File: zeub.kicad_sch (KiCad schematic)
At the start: 27 parts, among them J1 debug-port, J2 OLED-128x32, J5 Conn_01x03, J6 Conn_01x03, Q1 AO3401A, Q2 AO3401A, Q3 AO3401A, Q4 AO3401A, Q5 AO3401A, SW1 SKRHA, SW2 RotaryEncoder_Switch, U5 holyiot-18010-no-underside, U6 MT25QL128ABA1ESE

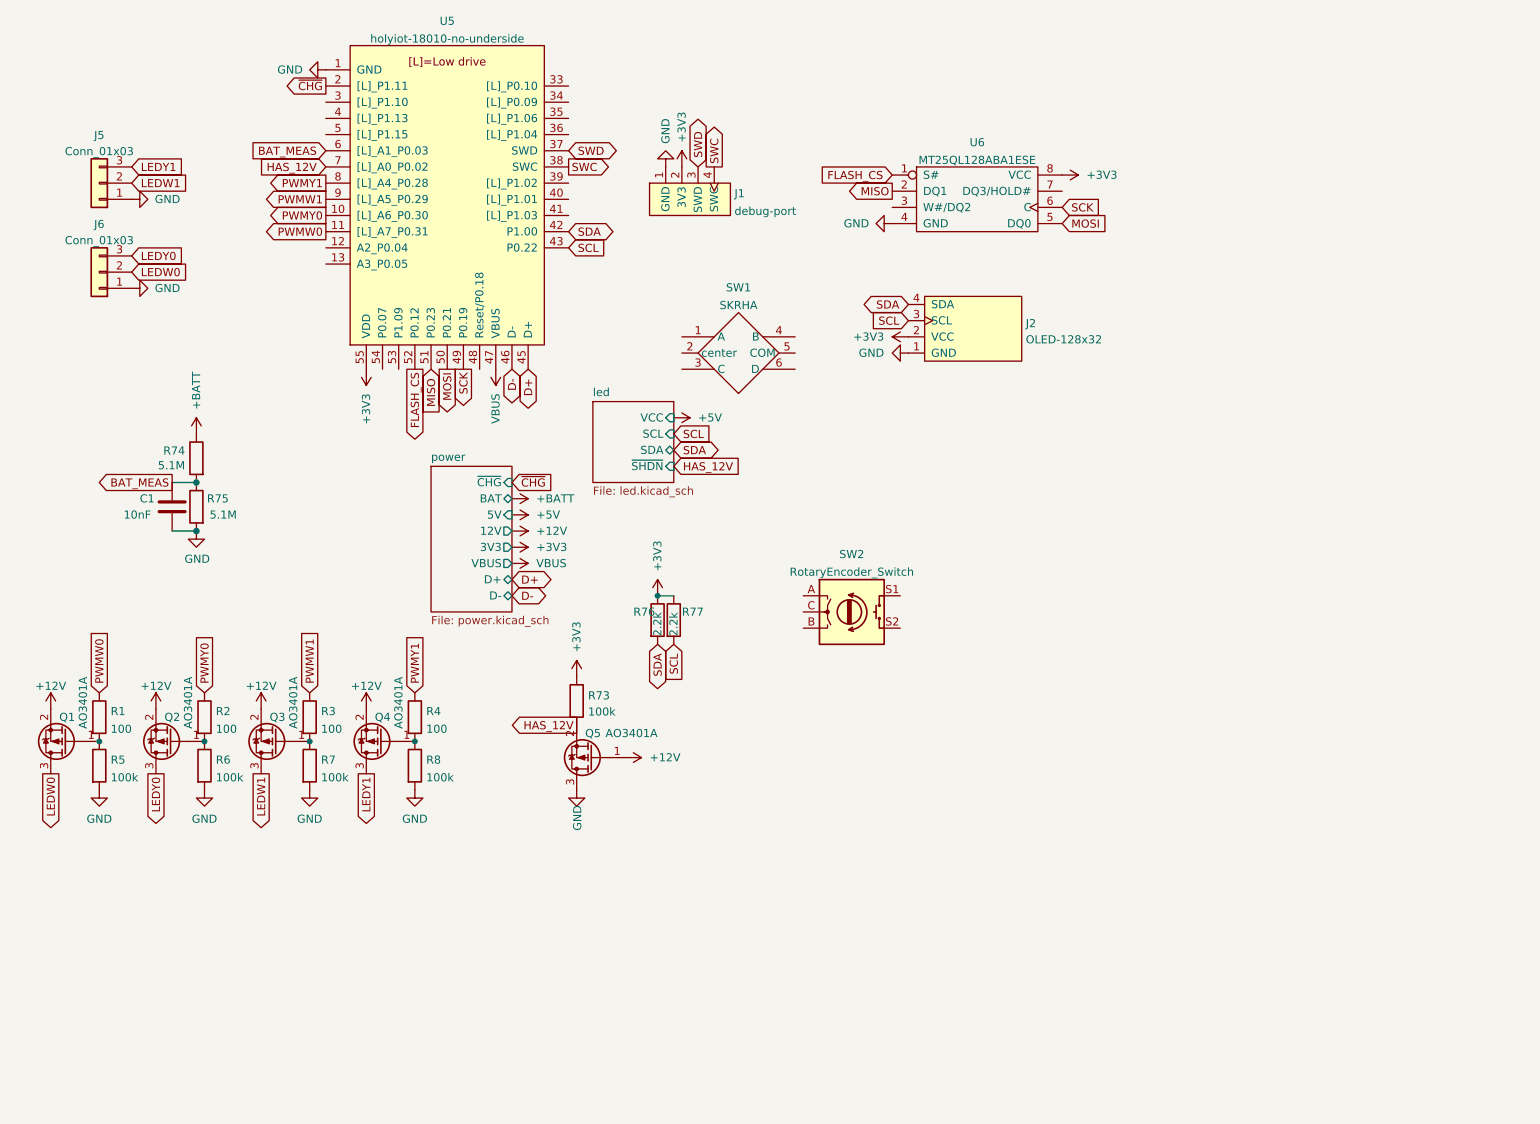
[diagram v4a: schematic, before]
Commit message: rid of LED driver resistors
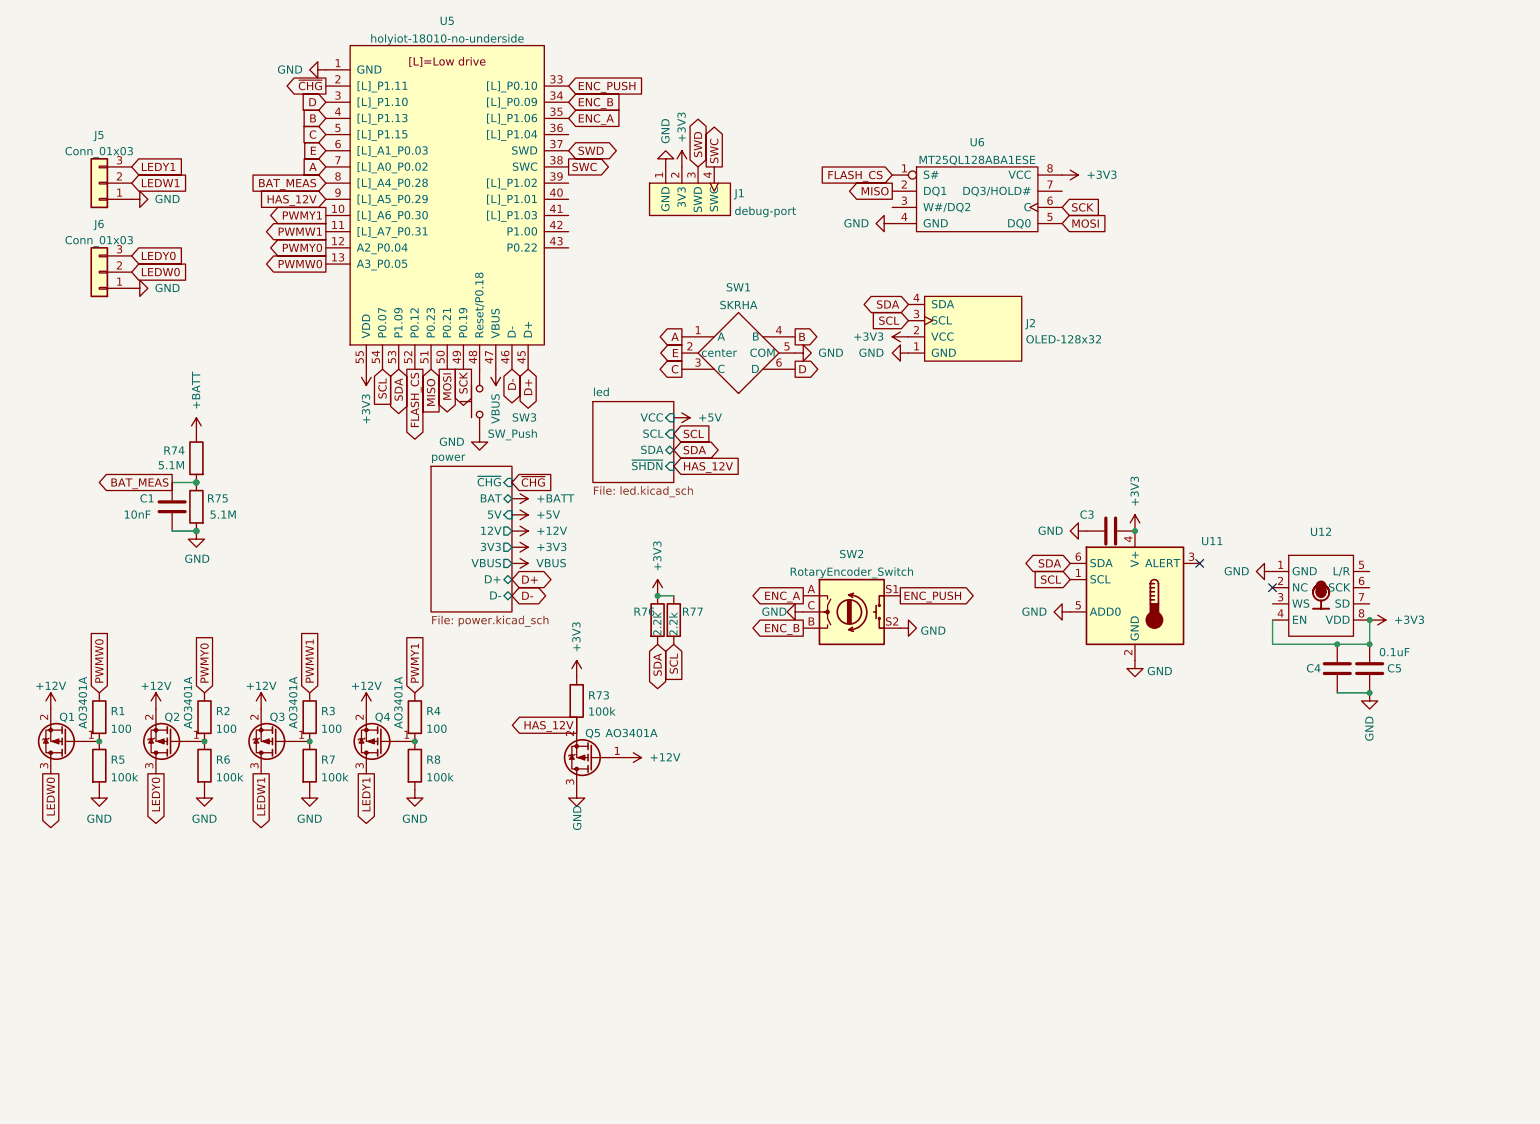
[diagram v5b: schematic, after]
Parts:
- added C3, C4: (no value), Capacitor_SMD:C_0603_1608Metric, symbol Device:C
- added C5: 0.1uF, Capacitor_SMD:C_0603_1608Metric, symbol Device:C
- added SW3: SW_Push, Button_Switch_SMD:SW_SPST_B3U-1000P, symbol Switch:SW_Push
- added U11: (no value), symbol ic:TMP117
- added U12: (no value), symbol ic:CMM4030D
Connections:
- net +3V3: now also C3.2, C4.2, C5.2, U11.4 (V+), U12.4 (EN), U12.8 (VDD)
- net BAT_MEAS: now also U5.8 ([L]_A4_P0.28); no longer U5.6 ([L]_A1_P0.03)
- net GND: now also SW1.5 (COM), SW2.C, SW2.S2, C3.1, C4.1, C5.1, SW3.1, U11.2 (GND), U11.5 (ADD0), U11.7 (GND), U12.1 (GND)
- net HAS_12V: now also U5.9 ([L]_A5_P0.29); no longer U5.7 ([L]_A0_P0.02)
- net PWMW0: now also U5.13 (A3_P0.05); no longer U5.11 ([L]_A7_P0.31)
- net PWMW1: now also U5.11 ([L]_A7_P0.31); no longer U5.9 ([L]_A5_P0.29)
- net PWMY0: now also U5.12 (A2_P0.04); no longer U5.10 ([L]_A6_P0.30)
- net PWMY1: now also U5.10 ([L]_A6_P0.30); no longer U5.8 ([L]_A4_P0.28)
- net SCL: now also U5.54 (P0.07), U11.1 (SCL); no longer U5.43 (P0.22)
- net SDA: now also U5.53 (P1.09), U11.6 (SDA); no longer U5.42 (P1.00)
- net A: now reaches SW1.1 (A)
- net A: now also U5.7 ([L]_A0_P0.02)
- net E: now reaches SW1.2 (center)
- net E: now also U5.6 ([L]_A1_P0.03)
- net C: now reaches SW1.3 (C)
- net C: now also U5.5 ([L]_P1.15)
- net B: now reaches SW1.4 (B)
- net B: now also U5.4 ([L]_P1.13)
- net D: now reaches SW1.6 (D)
- net D: now also U5.3 ([L]_P1.10)
- net ENC_A: now reaches SW2.A
- net ENC_A: now also U5.35 ([L]_P1.06)
- net ENC_B: now reaches SW2.B
- net ENC_B: now also U5.34 ([L]_P0.09)
- net ENC_PUSH: now reaches SW2.S1
- net ENC_PUSH: now also U5.33 ([L]_P0.10)
- net at U5.48 (Reset/P0.18): now also SW3.2
- no-connect marks 0 -> 2

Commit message: Added audio stuff; rerouted for prep
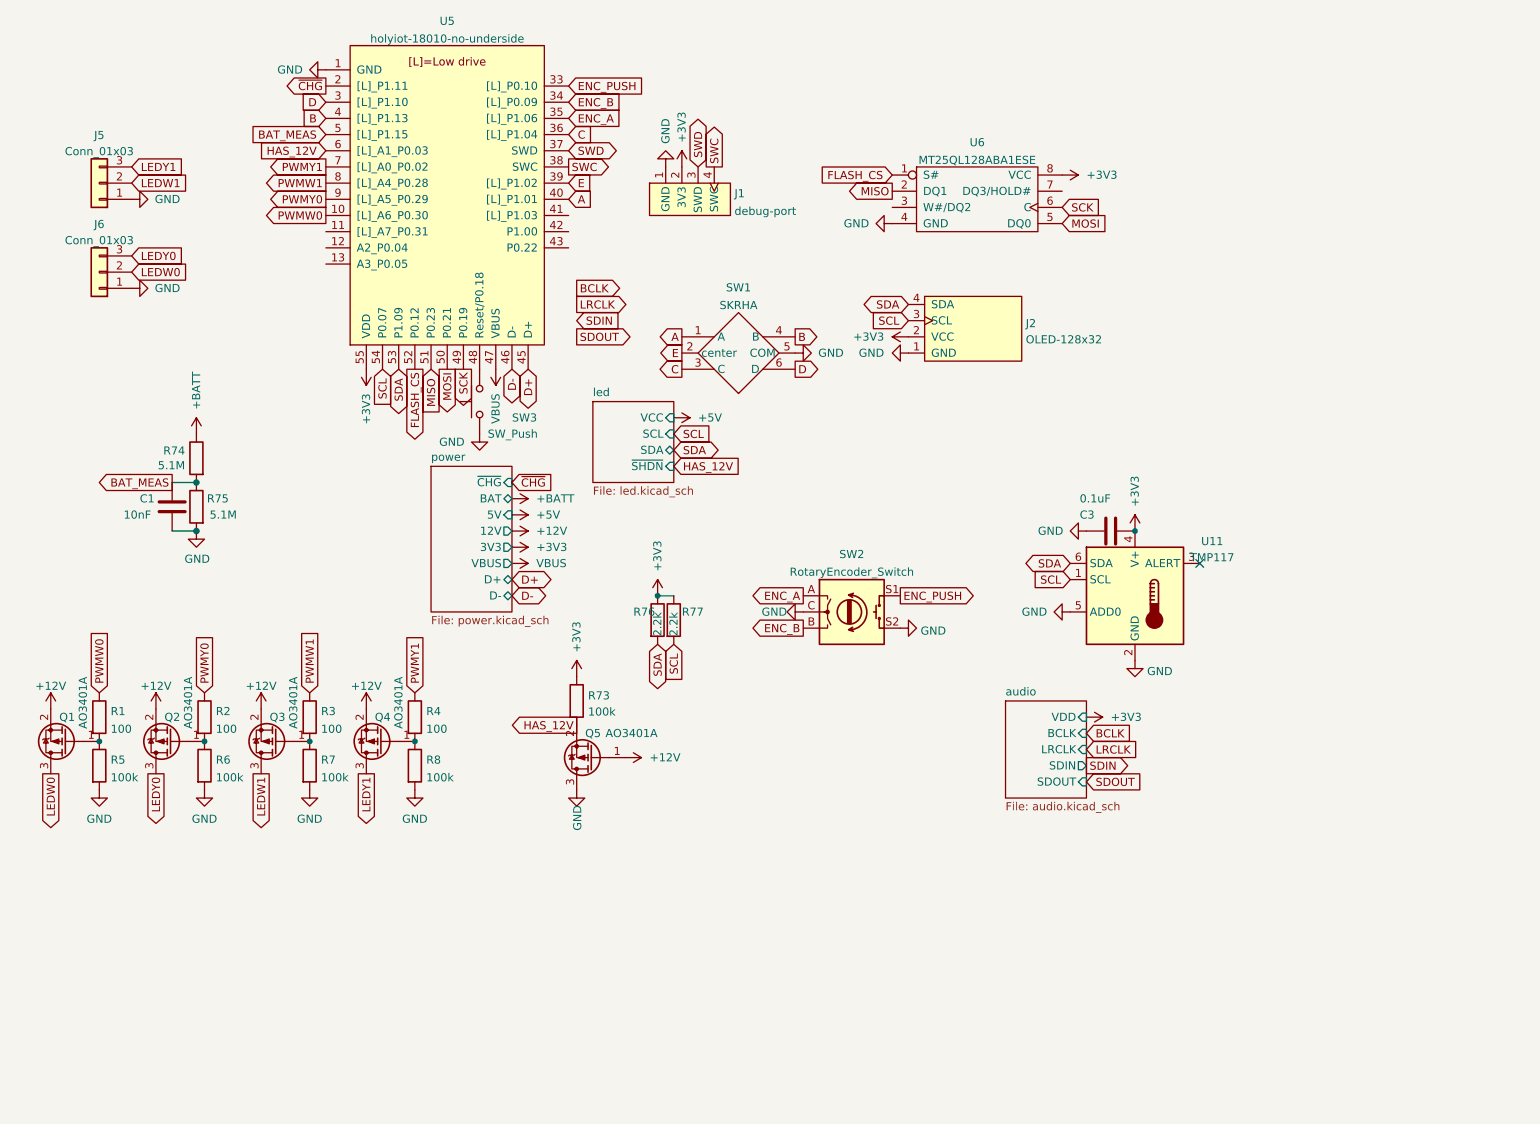
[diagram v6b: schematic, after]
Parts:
- removed C4: (no value), Capacitor_SMD:C_0603_1608Metric, symbol Device:C
- removed C5: 0.1uF, Capacitor_SMD:C_0603_1608Metric, symbol Device:C
- removed U12: (no value), symbol ic:CMM4030D
- C3: value (none) -> 0.1uF
- U11: value (none) -> TMP117; footprint (none) -> Package_SON:WSON-6-1EP_2x2mm_P0.65mm_EP1x1.6mm
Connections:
- net A: now also U5.40 ([L]_P1.01); no longer U5.7 ([L]_A0_P0.02)
- net BAT_MEAS: now also U5.5 ([L]_P1.15); no longer U5.8 ([L]_A4_P0.28)
- net C: now also U5.36 ([L]_P1.04); no longer U5.5 ([L]_P1.15)
- net E: now also U5.39 ([L]_P1.02); no longer U5.6 ([L]_A1_P0.03)
- net HAS_12V: now also U5.6 ([L]_A1_P0.03); no longer U5.9 ([L]_A5_P0.29)
- net PWMW0: now also U5.10 ([L]_A6_P0.30); no longer U5.13 (A3_P0.05)
- net PWMW1: now also U5.8 ([L]_A4_P0.28); no longer U5.11 ([L]_A7_P0.31)
- net PWMY0: now also U5.9 ([L]_A5_P0.29); no longer U5.12 (A2_P0.04)
- net PWMY1: now also U5.7 ([L]_A0_P0.02); no longer U5.10 ([L]_A6_P0.30)
- no-connect marks 2 -> 1
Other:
- added sheet audio (audio.kicad_sch)

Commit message: fully routed
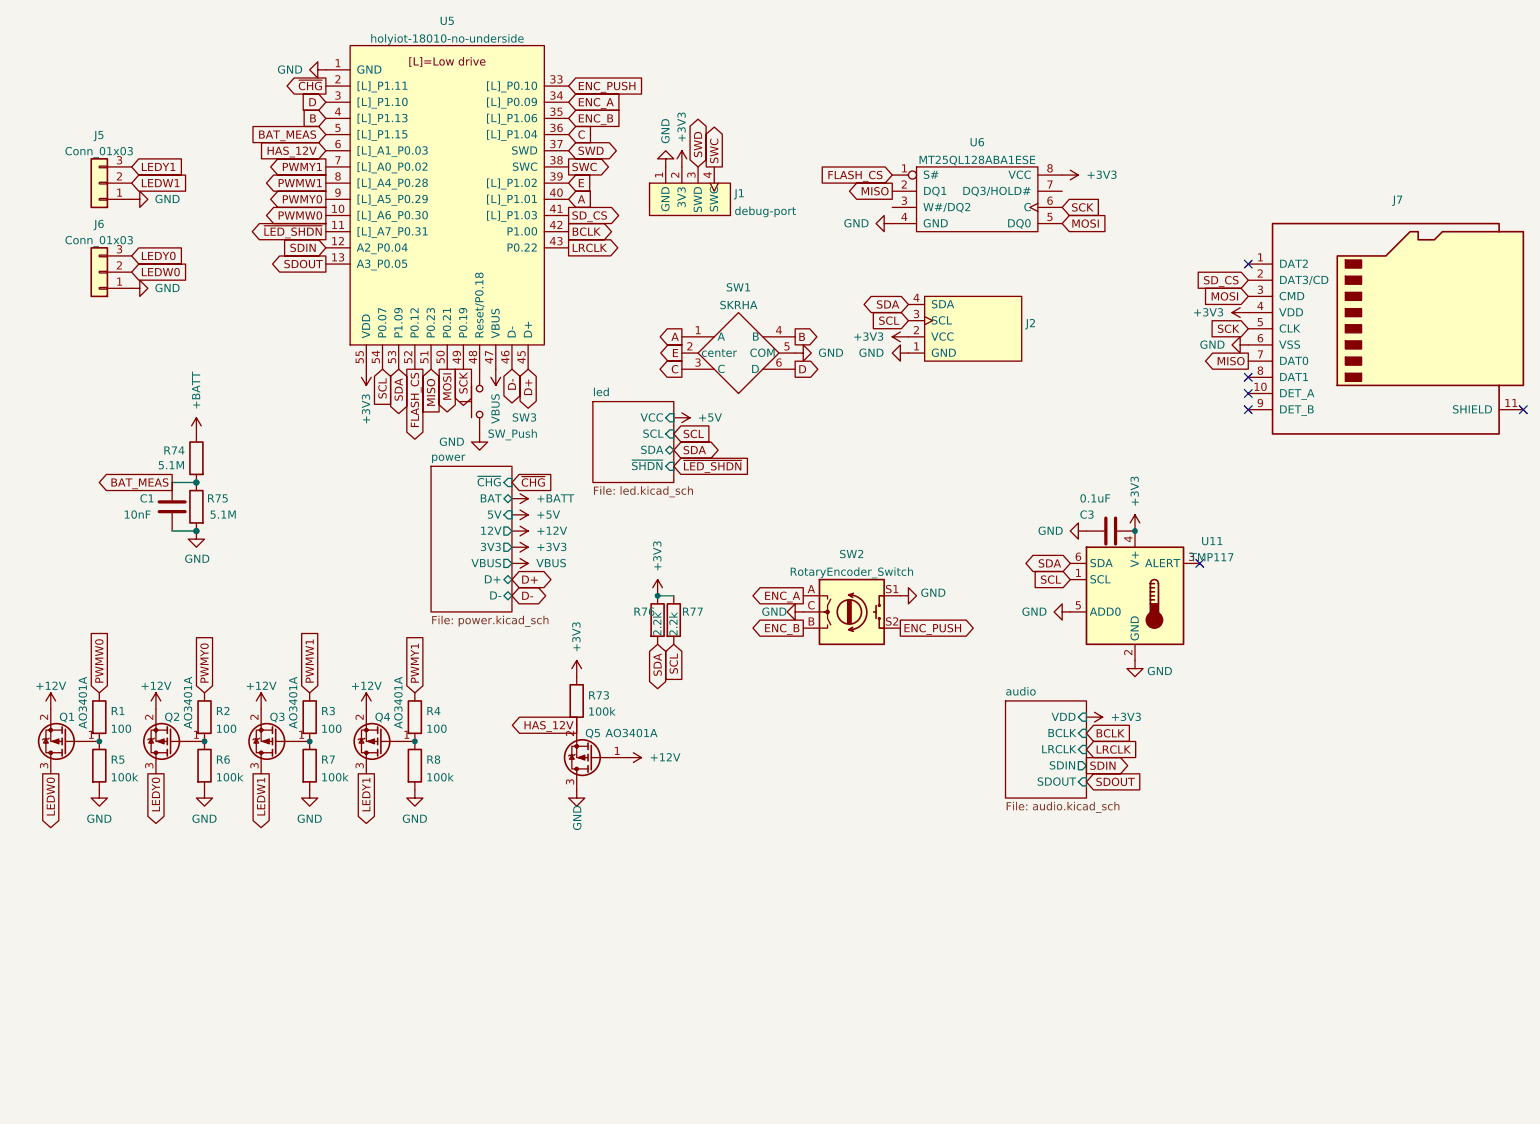
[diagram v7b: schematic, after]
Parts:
- added J7: (no value), symbol Connector:Micro_SD_Card_Det
- J2: value OLED-128x32 -> (none); footprint display:OLED-128x32-cutout -> (none)
- SW2: footprint Rotary_Encoder:RotaryEncoder_Alps_EC12E-Switch_Vertical_H20mm_CircularMountingHoles -> (none)
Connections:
- net +3V3: now also J7.4 (VDD)
- net BCLK: now also U5.42 (P1.00)
- net ENC_A: now also U5.34 ([L]_P0.09); no longer U5.35 ([L]_P1.06)
- net ENC_B: now also U5.35 ([L]_P1.06); no longer U5.34 ([L]_P0.09)
- net ENC_PUSH: now also SW2.S2; no longer SW2.S1
- net GND: now also SW2.S1, J7.6 (VSS); no longer SW2.S2
- net LRCLK: now also U5.43 (P0.22)
- net MISO: now also J7.7 (DAT0)
- net MOSI: now also J7.3 (CMD)
- net SCK: now also J7.5 (CLK)
- net SDIN: now also U5.12 (A2_P0.04)
- net SDOUT: now also U5.13 (A3_P0.05)
- net ~{LED_SHDN}: now reaches U5.11 ([L]_A7_P0.31)
- net SD_CS: now reaches U5.41 ([L]_P1.03)
- net SD_CS: now also J7.2 (DAT3/CD)
- no-connect marks 1 -> 6

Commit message: first version
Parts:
- removed Q1, Q2, Q3, Q4, Q5: AO3401A, Package_TO_SOT_SMD:SOT-23, symbol Transistor_FET:AO3401A
- added Q1, Q2, Q3, Q4, Q5: AO3400A, Package_TO_SOT_SMD:SOT-23, symbol Transistor_FET:AO3400A
- added Q6, Q7, Q8, Q9: AO3401A, Package_TO_SOT_SMD:SOT-23, symbol Transistor_FET:AO3401A
- added R19, R20, R21: 10k, Resistor_SMD:R_0603_1608Metric, symbol Device:R
- added R22: 100k, Resistor_SMD:R_0603_1608Metric, symbol Device:R
- J2: value (none) -> OLED-128x32; footprint (none) -> display:OLED-128x64
- J7: value (none) -> Micro_SD_Card_Det; footprint (none) -> misc:molex-503182-1852
- R5: value 100k -> 10k
- SW2: footprint (none) -> switch:EVQWGD001
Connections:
- net +12V: now also R5.1, Q5.1 (G), Q6.2 (S), Q7.2 (S), Q8.2 (S), Q9.2 (S), R19.1, R20.1, R21.1
- net GND: now also Q1.2 (S), Q2.2 (S), Q3.2 (S), Q4.2 (S), Q5.2 (S), R22.2; no longer R5.2
- net HAS_12V: now also Q5.3 (D)
- net LEDW0: now also Q6.3 (D)
- net LEDW1: now also Q8.3 (D)
- net LEDY0: now also Q7.3 (D)
- net LEDY1: now also Q9.3 (D)
- net at R1.2: now also Q1.1 (G), R22.1; no longer R5.1
- net at R3.2, R7.1: now also Q3.1 (G)
- net at R2.2, R6.1: now also Q2.1 (G)
- net at R4.2, R8.1: now also Q4.1 (G)
- new net: Q1.3 (D), Q6.1 (G), R5.2
- new net: Q4.3 (D), Q9.1 (G), R21.2
- new net: Q2.3 (D), Q7.1 (G), R19.2
- new net: Q3.3 (D), Q8.1 (G), R20.2
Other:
- moved on the sheet: R1, R2, R3, R4, R6, R7, R8
